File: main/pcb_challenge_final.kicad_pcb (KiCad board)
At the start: 2 copper layers, 164 parts, among them J4 Conn_01x04_Pin, J5 Conn_01x04_Pin, Q15 Q_Dual_NPN_PNP_B1E2B2C2E1C1, Q16 Q_Dual_NPN_PNP_B1E2B2C2E1C1, Q17 Q_Dual_NPN_PNP_B1E2B2C2E1C1, Q18 Q_Dual_NPN_PNP_B1E2B2C2E1C1, Q19 Q_Dual_NPN_PNP_B1E2B2C2E1C1, Q20 Q_Dual_NPN_PNP_B1E2B2C2E1C1, Q21 Q_Dual_NPN_PNP_B1E2B2C2E1C1, Q22 Q_Dual_NPN_PNP_B1E2B2C2E1C1, Q23 Q_Dual_NPN_PNP_B1E2B2C2E1C1, Q24 Q_Dual_NPN_PNP_B1E2B2C2E1C1, Q25 Q_Dual_NPN_PNP_B1E2B2C2E1C1, Q26 Q_Dual_NPN_PNP_B1E2B2C2E1C1, Q27 Q_Dual_NPN_PNP_B1E2B2C2E1C1, Q28 Q_Dual_NPN_PNP_B1E2B2C2E1C1, Q29 Q_Dual_NPN_PNP_B1E2B2C2E1C1, SW1 SW_Push, SW2 SW_Push, SW3 SW_Push, U1 74AUP1G80, U10 NMUX1308BQ, U11 NMUX1308BQ, U12 NMUX1308BQ, U13 NMUX1308BQ, U14 NMUX1308BQ, U15 NMUX1308BQ, U16 NMUX1308BQ, U17 74AUP1G80, U18 74AHC1G86, U19 74AUP1G80, U20 74AUP1G80, U21 74LV1T08GV, U22 CD74HC283M96, U23 74LV1T08GV, U24 74LVC1GU04DRL, U25 ESP32-S3-MINI-1, U26 74LVC1GU04DRL, U27 74LV1T08GV, U28 CD74HC283M96, U29 NMUX1308BQ, U3 74AHC1G86, U30 NMUX1308BQ, U31 NMUX1308BQ, U32 NMUX1308BQ, U33 74AUP1G80, U34 74AUP1G80, U35 NMUX1308BQ, U36 NMUX1308BQ, U37 74AUP1G80, U38 74AUP1G80, U39 NMUX1308BQ, U4 74AUP1G80, U40 NMUX1308BQ, U41 NMUX1308BQ, U42 NMUX1308BQ, U43 NMUX1308BQ, U44 NMUX1308BQ, U45 74AUP1G80, U46 74AUP1G80, U47 74AUP1G80, U48 74AUP1G80, U49 74AUP1G80, U5 74AUP1G80, U50 74AUP1G80, U51 74LV1T08GV, U52 74AHC1G86, U53 74LVC1GU04DRL, U54 74LVC1GU04DRL, U55 74AHC1G86, U56 74AHC1G86, U57 74LVC1GU04DRL, U58 74LVC1GU04DRL, U59 74LV1T08GV, U6 74AUP1G80, U60 74AHC1G86, U61 74LVC1GU04DRL, U62 74LV1T08GV, U63 74LV1T08GV, U64 NMUX1308BQ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

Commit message: PCB Challenge 2026 submission - Mickey
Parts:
- C13, C14, Q16, Q19, Q20, Q21, Q22, Q24, Q25, Q26, Q27, R24, R31, R32, R34, R35, R36, R37, R38, R41, R42, R44, R45, R47, R49, R6, R61, R62, R63, R64, R65, R66, R67, R68, R7, U10, U14, U15, U16, U17, U19, U20, U28, U30, U37, U4, U5, U9, Y2: moved to B.Cu
- moved SW1 89.8 mm to (144.7, 77.5)
- moved R1 85.3 mm to (172.2, 76.9), turned to 180 degrees
- moved C8 84.7 mm to (169.9, 77.2), turned to -90 degrees
- moved C7 82.8 mm to (170.7, 77.2), turned to -90 degrees
- moved C2 80.3 mm to (153.1, 78.1), turned to 90 degrees
- moved U61 80.2 mm to (138.9, 81.3), turned to 90 degrees
- moved C1 79.2 mm to (152.2, 78.1), turned to 90 degrees
- moved SW3 75.8 mm to (172.0, 83.8), turned to -90 degrees
- moved SW2 73.9 mm to (158.3, 103.6)
- moved U58 73.9 mm to (140.0, 84.8), turned to 90 degrees
- moved C6 71.2 mm to (161.2, 91.1), turned to 180 degrees
- moved U65 69.8 mm to (150.1, 84.5)
- moved C5 69.0 mm to (162.7, 91.1)
- moved U22 68.8 mm to (125.0, 89.7), turned to 180 degrees
- moved U45 68.4 mm to (135.8, 81.9), turned to 180 degrees
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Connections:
- C9 pad 1: rst -> NRST
- SW2 pad 2: rst -> NRST
- U22 pad 9: COUT -> (no net)
- U25 pad 2: Net-(U25-GND-Pad2) -> GND
- U25 pad 42: Net-(U25-GND-Pad2) -> GND
- U25 pad 43: Net-(U25-GND-Pad2) -> GND
- U25 pad 46: Net-(U25-GND-Pad2) -> GND
- U25 pad 47: Net-(U25-GND-Pad2) -> GND
- U25 pad 48: Net-(U25-GND-Pad2) -> GND
- U25 pad 49: Net-(U25-GND-Pad2) -> GND
- U25 pad 50: Net-(U25-GND-Pad2) -> GND
- U25 pad 51: Net-(U25-GND-Pad2) -> GND
- U25 pad 52: Net-(U25-GND-Pad2) -> GND
- U25 pad 53: Net-(U25-GND-Pad2) -> GND
- U25 pad 54: Net-(U25-GND-Pad2) -> GND
- U25 pad 55: Net-(U25-GND-Pad2) -> GND
- U25 pad 56: Net-(U25-GND-Pad2) -> GND
- U25 pad 57: Net-(U25-GND-Pad2) -> GND
- U25 pad 58: Net-(U25-GND-Pad2) -> GND
- U25 pad 59: Net-(U25-GND-Pad2) -> GND
- U25 pad 60: Net-(U25-GND-Pad2) -> GND
- U25 pad 61: Net-(U25-GND-Pad2) -> GND
- U25 pad 62: Net-(U25-GND-Pad2) -> GND
- U25 pad 63: Net-(U25-GND-Pad2) -> GND
- U25 pad 64: Net-(U25-GND-Pad2) -> GND
- U25 pad 65: Net-(U25-GND-Pad2) -> GND
- U28 pad 9: COUT -> (no net)
- Y2 pad 1: EN -> en
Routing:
- net +3.3V: track 0.00 -> 460.3 mm, vias 0 -> 65
- net GND: track 0.00 -> 292.8 mm, vias 0 -> 101
- net IO6: track 0.00 -> 141.3 mm, vias 0 -> 16
- net IO8: track 0.00 -> 140.4 mm, vias 0 -> 9
- net rst: track 0.00 -> 127.0 mm, vias 0 -> 7
- net clk: track 0.00 -> 112.8 mm, vias 0 -> 4
- net wr1: track 0.00 -> 106.8 mm, vias 0 -> 1
- net rw1: track 0.00 -> 74.6 mm, vias 0 -> 1
- net R_en: track 0.00 -> 66.5 mm, vias 0 -> 3
- net r_en: track 0.00 -> 59.8 mm, vias 0 -> 4
- net rc1: track 0.00 -> 42.0 mm, vias 0 -> 3
- net rc2: track 0.00 -> 39.9 mm, vias 0 -> 3
- net wr2: track 0.00 -> 37.0 mm, vias 0 -> 3
- net wr3: track 0.00 -> 35.5 mm, vias 0 -> 2
- net rc3: track 0.00 -> 31.4 mm, vias 0 -> 2
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- added copper zone on B.Cu, net +3.3V
- added copper zone on In2.Cu, net +3.3V
- added copper zone on B.Cu, net GND
- added copper zone on F.Cu, net GND
- added copper zone on In1.Cu, net GND
- added copper zone on In2.Cu, net GND
- added copper zone on B.Cu, net Net-(J3-SHIELD)
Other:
- board outline added: 62.2 x 46.8 mm
- copper layers 2 -> 4

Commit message: small changes
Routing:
- net clk: track 112.8 -> 118.9 mm
- net r_en: track 59.8 -> 59.2 mm
- net ???: track 8.54 -> 9.08 mm

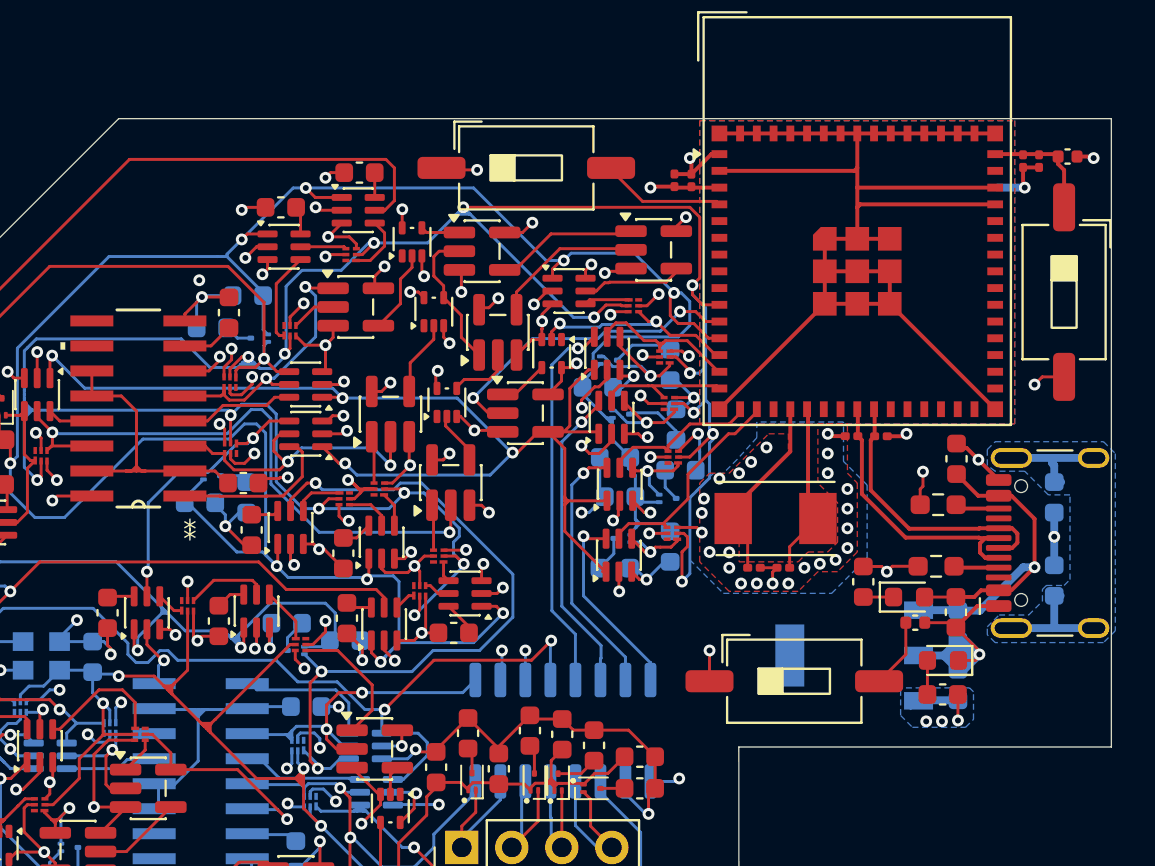
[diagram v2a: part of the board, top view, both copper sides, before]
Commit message: DRC fix
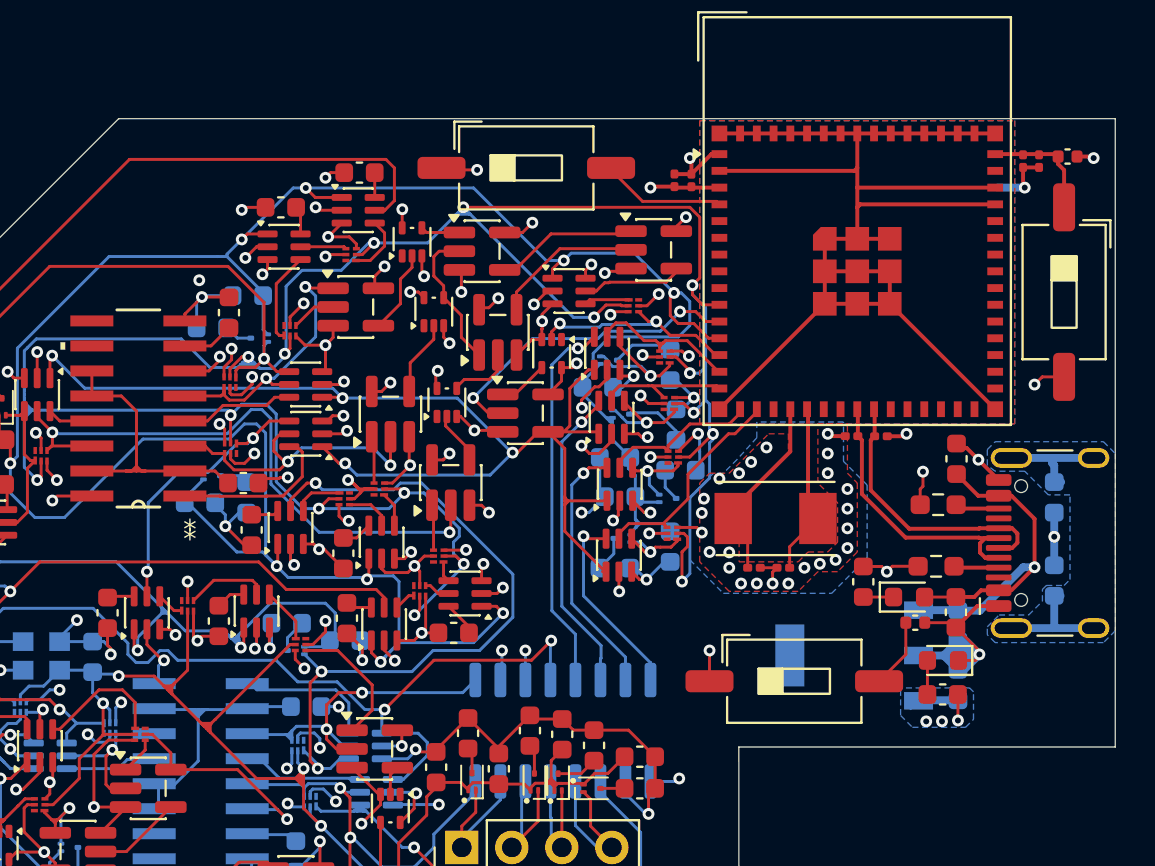
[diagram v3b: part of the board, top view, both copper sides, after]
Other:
- board size 62.2 x 46.8 mm -> 62.4 x 46.8 mm
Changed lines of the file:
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@@
 	(gr_poly
 		(pts
-			(xy 174.4 106.9) (xy 155.484586 106.9) (xy 155.496563 121.8) (xy 112.2 121.8) (xy 112.2 86.8) (xy 124 75)
-			(xy 174.4 75)
+			(xy 174.6 106.9) (xy 155.484586 106.9) (xy 155.496563 121.8) (xy 112.2 121.8) (xy 112.2 86.8) (xy 124 75)
+			(xy 174.6 75)
 		)
 		(stroke
